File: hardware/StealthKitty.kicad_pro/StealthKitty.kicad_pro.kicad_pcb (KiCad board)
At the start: 4 copper layers, 54 x 57 mm, 77 parts, among them IC501 MP1475DJ-LF-P, J201 Conn_01x06, J202 Conn_01x06, J302 Conn_01x06, SW501 Switch, U301 ADXL343, U401 STM32G431CBU6

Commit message: Dernier Modif ROUTAGE 10/10/24
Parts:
- moved PWM1 CH2 0.50 mm to (143.9, 83.6)
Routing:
- net SDA: track 44.3 -> 38.1 mm, vias 4 -> 2
- net INT1_adx: track 11.2 -> 13.3 mm, vias 2 -> 1
- net PWM_MOT2_CH2: track 8.42 -> 9.60 mm
- net +3.3V: track 24.3 -> 23.5 mm
- net /brain Sheet/SWCLK: track 26.4 -> 27.2 mm
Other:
- board size 54 x 57 mm -> 53.9 x 57 mm

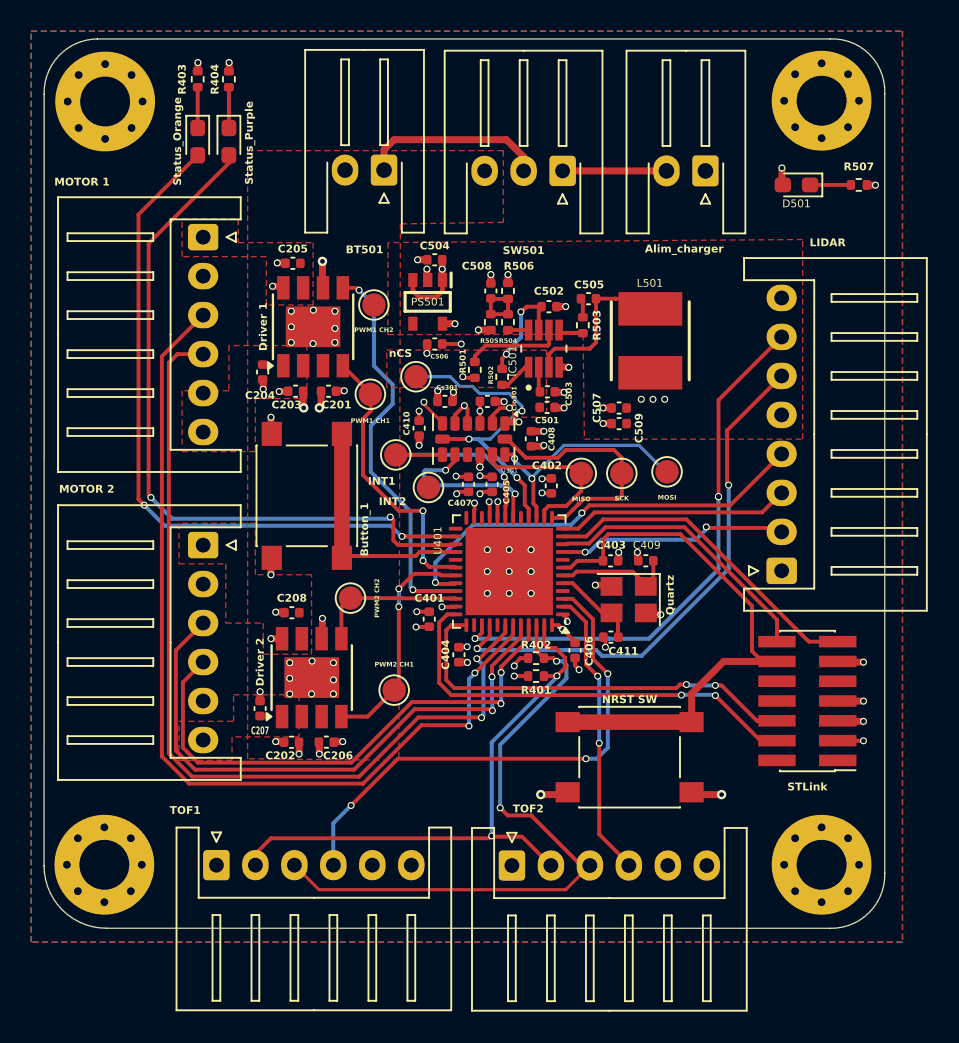
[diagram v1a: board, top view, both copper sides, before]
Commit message: Amélioration de la partie routage
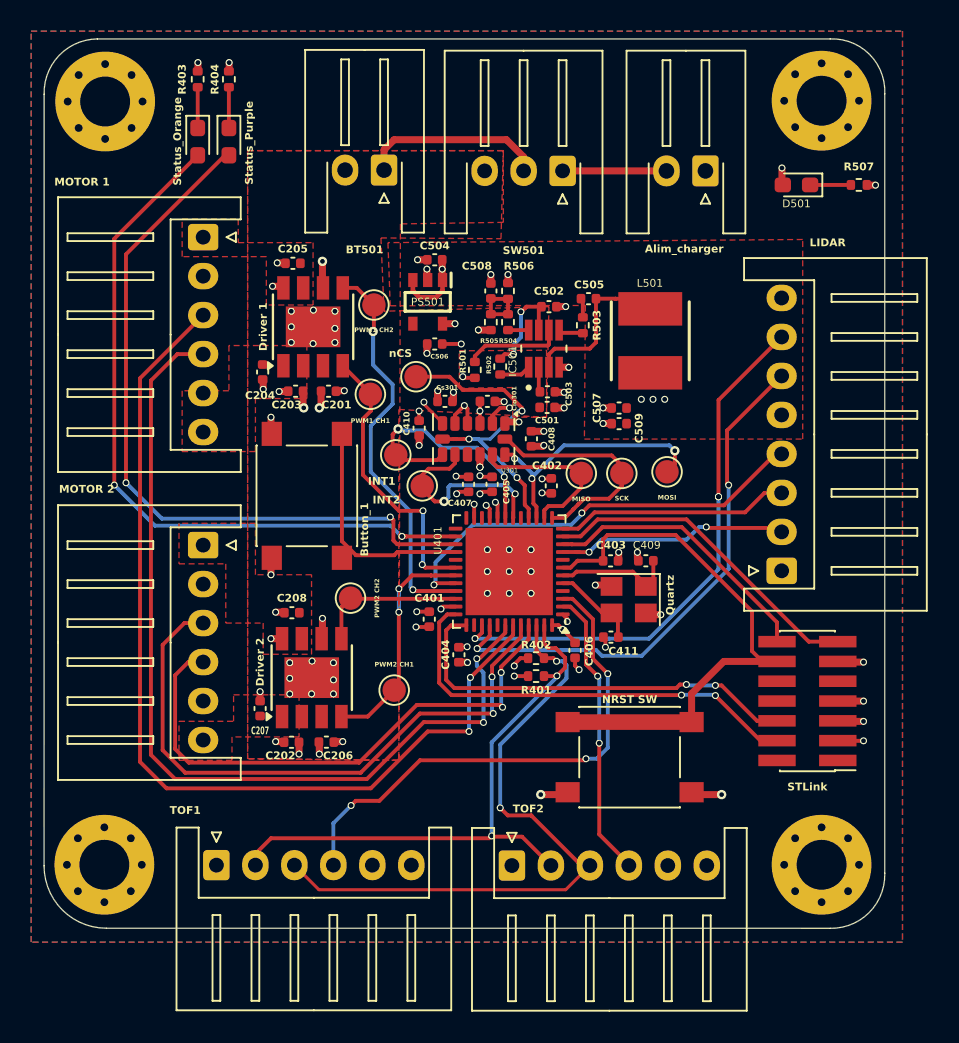
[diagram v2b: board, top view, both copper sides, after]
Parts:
- moved R502 0.67 mm to (152.0, 87.5)
- moved INT2 0.41 mm to (147.0, 95.2)
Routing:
- net INT1_adx: track 13.3 -> 16.0 mm, vias 1 -> 2
- net Codeur1_PH2: track 59.1 -> 61.6 mm
- net Codeur2_PH1: track 37.6 -> 39.8 mm
- net Codeur1_PH1: track 56.8 -> 58.7 mm
- net MOSI: track 15.5 -> 17.2 mm, vias 2 -> 3
- net /brain Sheet/status_Purple: track 45.8 -> 47.5 mm
- net /brain Sheet/status_Orange: track 45.0 -> 46.6 mm
- net Codeur2_PH2: track 34.2 -> 35.9 mm
- net INT2_adx: track 11.2 -> 12.8 mm
- net SCK: track 15.9 -> 14.8 mm
- net PWM_MOT2_CH2: track 9.60 -> 10.4 mm
- net /brain Sheet/Button_1: track 15.4 -> 14.8 mm
